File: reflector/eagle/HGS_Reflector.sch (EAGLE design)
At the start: 27 parts, among them J1 U.FL, U3 LP2985XX-N

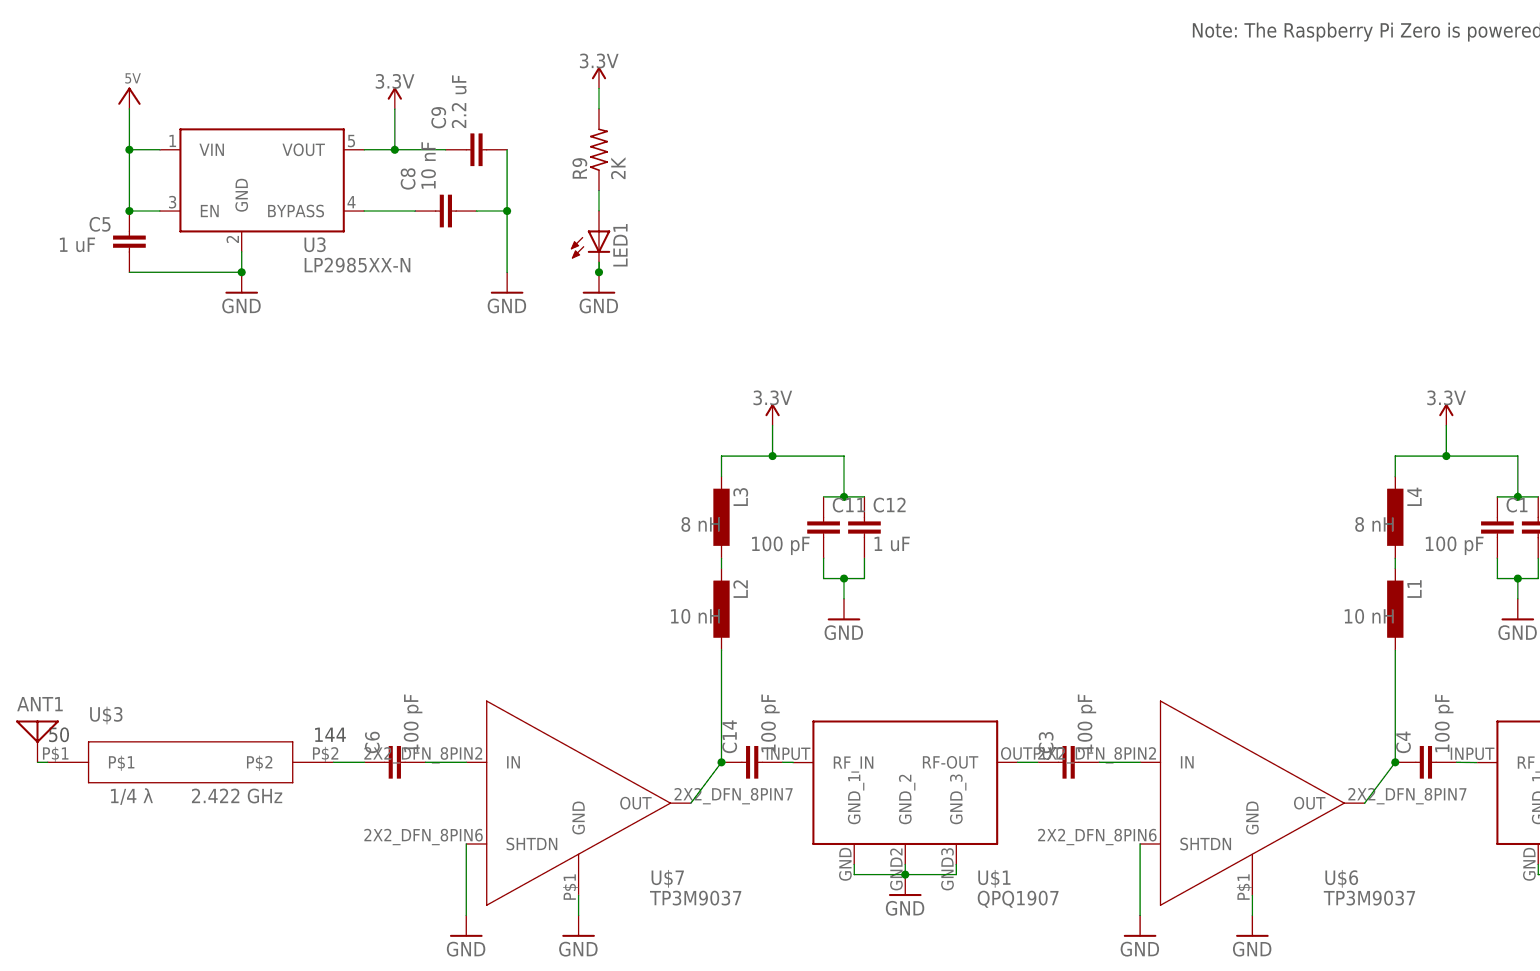
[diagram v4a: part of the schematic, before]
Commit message: Since the team working on HGS decided to switch from a 2 layer board to a 4 layer board, I began laying out the HGS parts on a new board with 4 layers. Currently, I have a number of questions regarding the layout to go over at the 11/29 structure meeting.
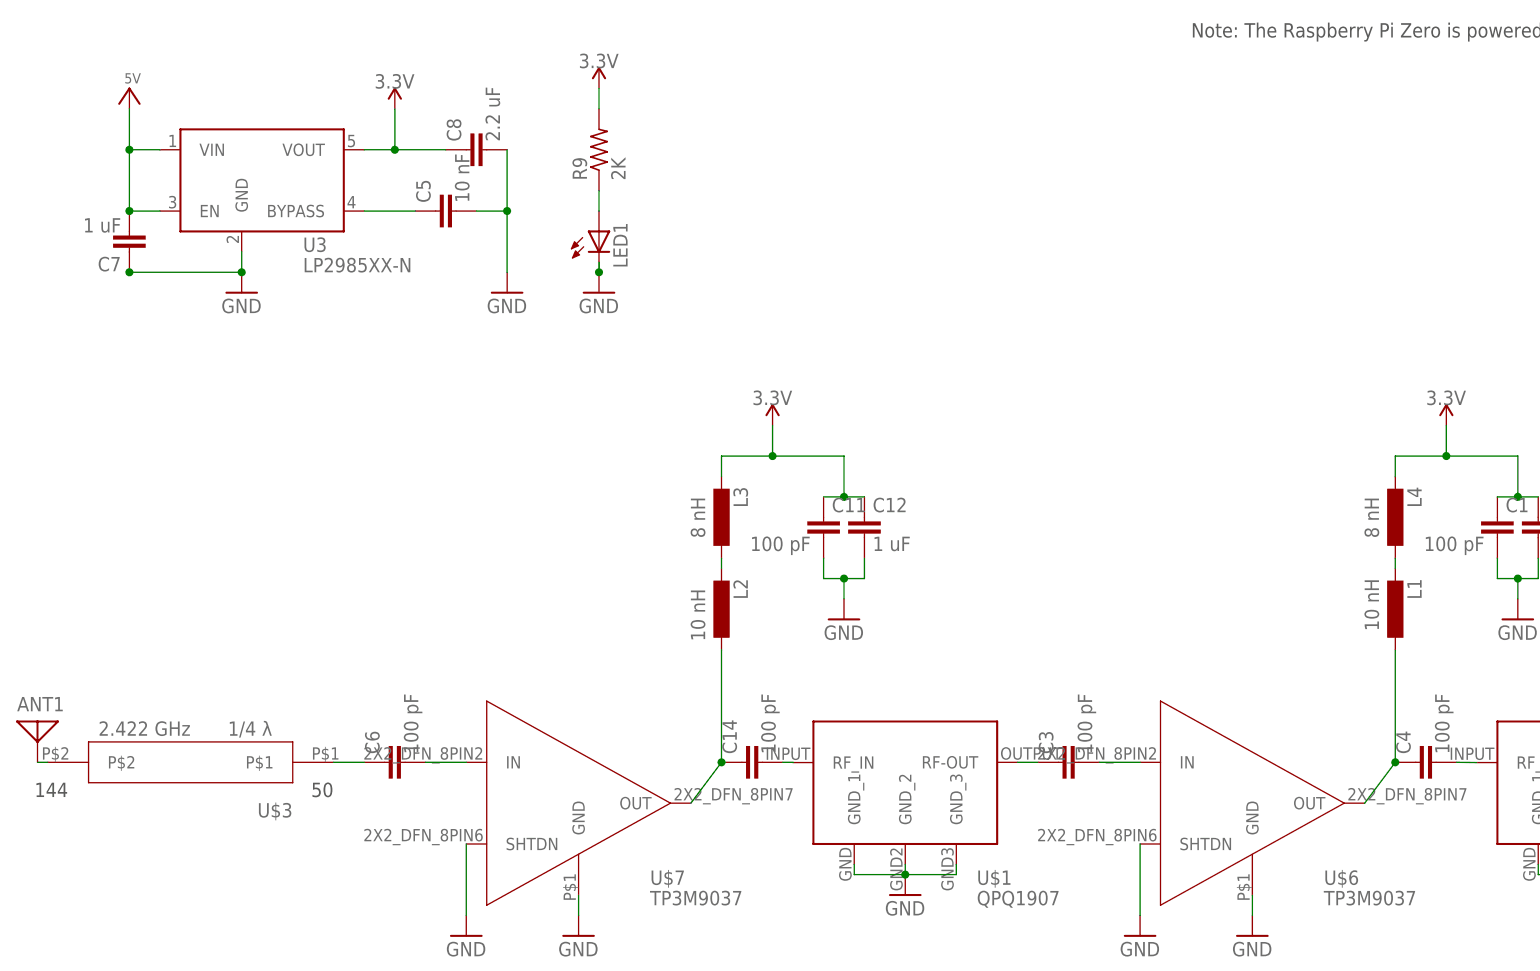
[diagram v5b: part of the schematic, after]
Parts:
- removed C9: 2.2 uF, ngspice-simulation:C
- added C7: 1 uF, oresat-rcl:C-EU0402-C-NOSILK
- C5: value 1 uF -> 10 nF; device ngspice-simulation:C -> oresat-rcl:C-EU0402-C-NOSILK; _EXTERNAL_ 1 uF -> (none)
- C8: value 10 nF -> 2.2 uF; device ngspice-simulation:C -> oresat-rcl:C-EU0402-C-NOSILK
- L1: IMPEDANCE (none) -> 10 nH; SPICEPREFIX 10 nH -> (none)
- L3, L4: IMPEDANCE (none) -> 8 nH; SPICEPREFIX 8 nH -> (none)
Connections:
- removed net N$12: ANT1.1, U$3.P$1
- new net N$2: ANT1.1, U$3.P$2
- net 3.3V: now also C8.1; no longer C9.1
- net 5V: now also C7.2; no longer C5.1
- net GND: now also C7.1; no longer C9.2
- net N$1: now also C5.1; no longer C8.1
- net N$9: now also U$3.P$1; no longer U$3.P$2
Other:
- moved on the sheet: U$3

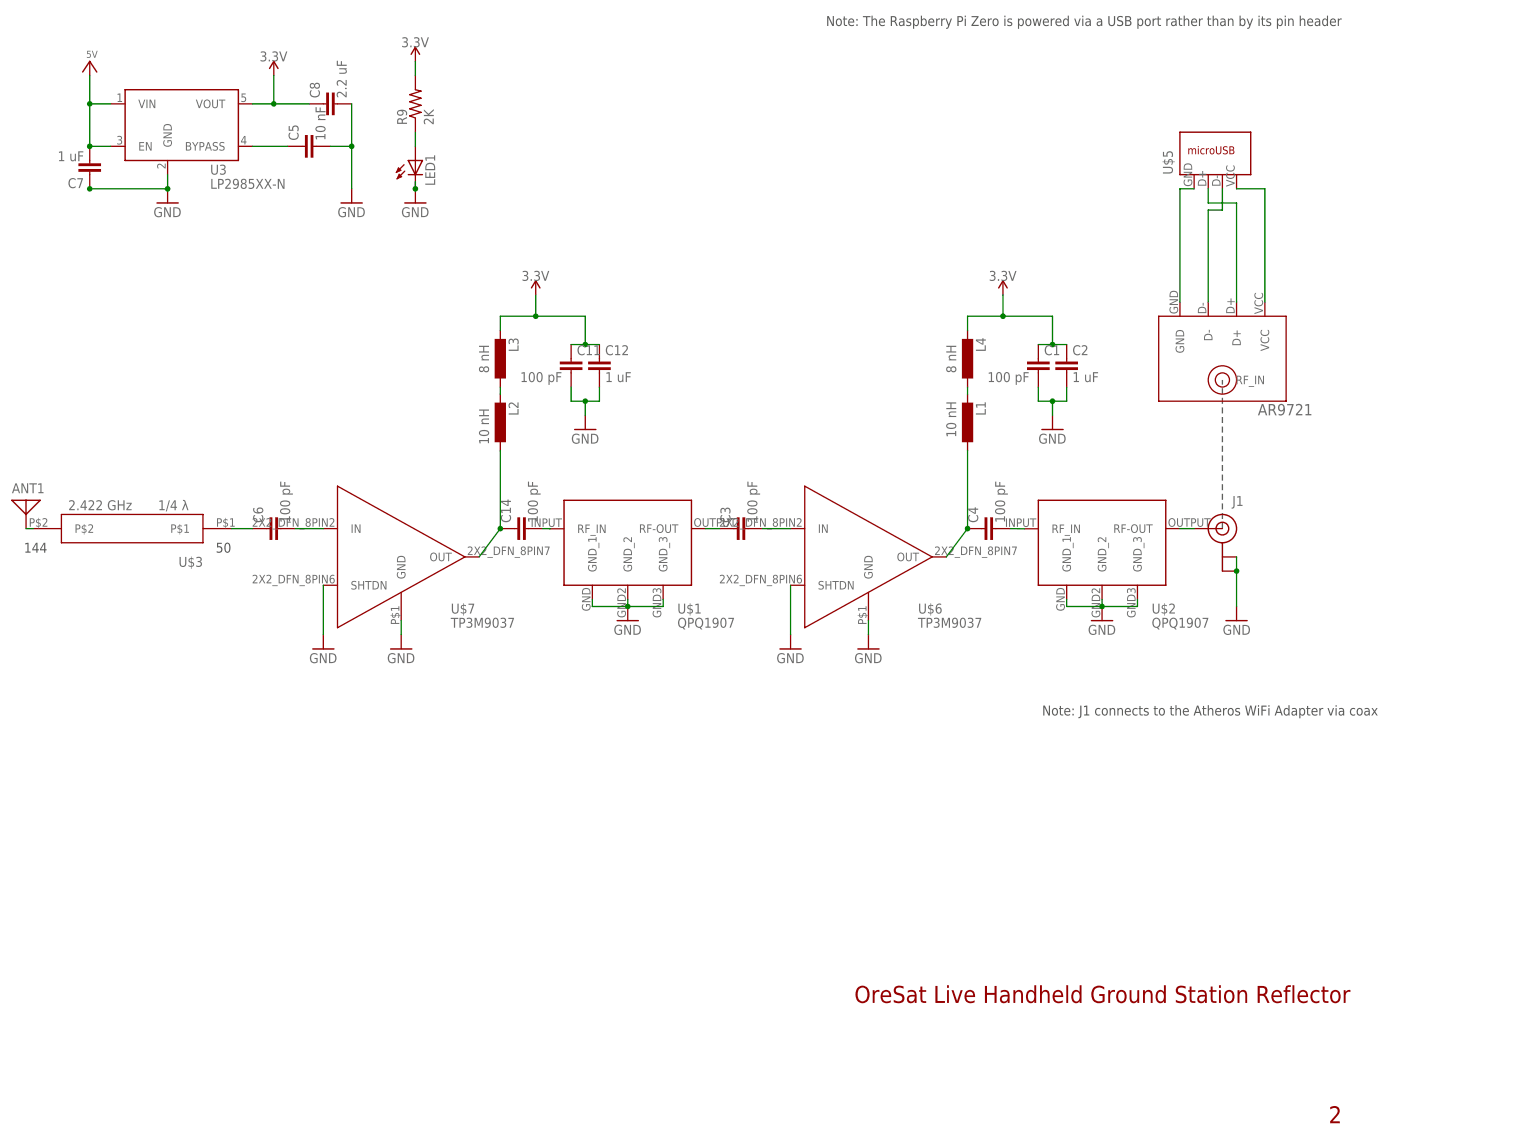
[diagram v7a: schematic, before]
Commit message: I finalized the schematic and routing of the board for HGS. Note that I adjusted the dxf layer by adding a fourth drill hole underneath the atheros card. It is ready for a design review.
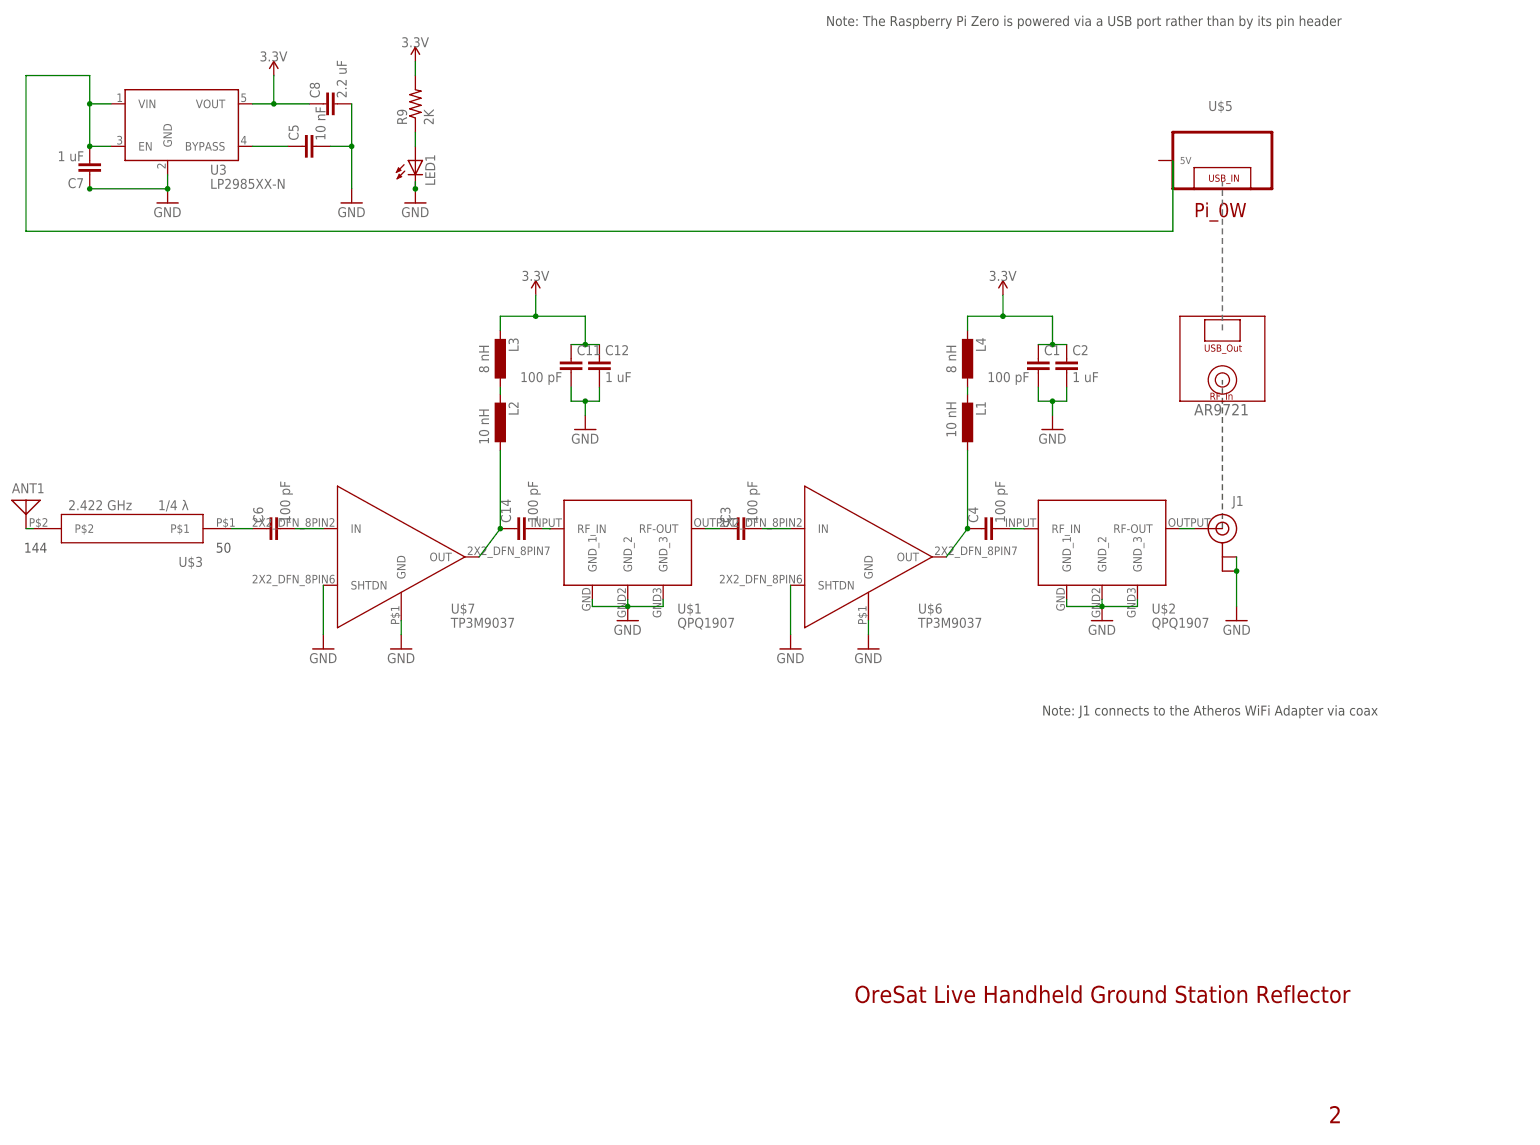
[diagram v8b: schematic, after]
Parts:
- U$4: value AR9721 -> AR9721WF; device AR9721:AR9721 -> AR9721:AR9721WF
- U$5: device Rasp_Pi_0W:RASP_PI_0W -> Rasp_Pi_0W:RASP_PI_0WPI_0W
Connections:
- removed net 1: U$4.GND
- removed net 5V: C7.2, U3.EN, U3.VIN
- removed net N$18: U$4.D+
- removed net N$19: U$4.D-
- removed net VCC: U$4.VCC
- new net N$12: C7.2, U$5.5V, U3.EN, U3.VIN
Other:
- moved on the sheet: U$5
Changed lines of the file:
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@@
 <part name="U3" library="U-TI-LP2985XX-N-linear-reg" deviceset="LP2985XX-N" device=""/>
 <part name="GND5" library="supply1" library_urn="urn:adsk.eagle:library:371" deviceset="GND" device=""/>
-<part name="3V-1" library="oresat-supplies" deviceset="5V" device=""/>
 <part name="GND1" library="supply1" library_urn="urn:adsk.eagle:library:371" deviceset="GND" device=""/>
 <part name="3.3V2" library="oresat-supplies" deviceset="3.3V" device=""/>
@@
 <part name="U$1" library="QPQ1907_BPF" deviceset="BPF" device=""/>
 <part name="U$2" library="QPQ1907_BPF" deviceset="BPF" device=""/>
-<part name="U$4" library="AR9721" deviceset="AR9721" device=""/>
-<part name="U$5" library="Rasp_Pi_0W" deviceset="RASP_PI_0W" device=""/>
+<part name="U$4" library="AR9721" deviceset="AR9721" device="WF"/>
+<part name="U$5" library="Rasp_Pi_0W" deviceset="RASP_PI_0W" device="PI_0W"/>
 <part name="U$3" library="TM-QWT-2.422GHz" deviceset="QWT2.422" device=""/>
 <part name="C7" library="oresat-rcl" deviceset="C-EU" device="0402-C-NOSILK" value="1 uF"/>
@@
 <text x="175.26" y="203.2" size="1.778" layer="97">Note: The Raspberry Pi Zero is powered via a USB port rather than by its pin header</text>
 <text x="274.32" y="81.28" size="1.778" layer="97" rot="R180">Note: J1 connects to the Atheros WiFi Adapter via coax</text>
-<wire x1="246.38" y1="113.03" x2="246.38" y2="139.7" width="0.1524" layer="97" style="shortdash"/>
+<wire x1="246.38" y1="113.03" x2="246.38" y2="139.7" width="0.254" layer="97" style="shortdash"/>
+<wire x1="246.38" y1="148.59" x2="246.38" y2="175.26" width="0.254" layer="95" style="shortdash"/>
 </plain>
 <instances>
@@
 <attribute name="VALUE" x="54.61" y="168.91" size="1.778" layer="96"/>
 </instance>
-<instance part="3V-1" gate="G$1" x="43.18" y="196.85" smashed="yes">
-<attribute name="VALUE" x="42.545" y="197.485" size="1.27" layer="96"/>
-</instance>
 <instance part="GND1" gate="1" x="99.06" y="91.44" smashed="yes">
 <attribute name="VALUE" x="96.52" y="88.9" size="1.778" layer="96"/>
@@
 </instance>
 <instance part="U$4" gate="G$1" x="246.38" y="143.51" smashed="yes"/>
-<instance part="U$5" gate="G$1" x="246.38" y="179.07" smashed="yes" rot="R90">
-<attribute name="NAME" x="237.49" y="176.53" size="1.778" layer="95" rot="R90"/>
-<attribute name="VALUE" x="254" y="176.53" size="1.778" layer="96" rot="R90"/>
+<instance part="U$5" gate="G$1" x="246.38" y="179.07" smashed="yes">
+<attribute name="NAME" x="243.84" y="187.96" size="1.778" layer="95"/>
+<attribute name="VALUE" x="243.84" y="171.45" size="1.778" layer="96"/>
 </instance>
 <instance part="U$3" gate="G$1" x="50.8" y="113.03" smashed="yes" rot="R180">
@@
 </segment>
 </net>
-<net name="1" class="0">
-<segment>
-<wire x1="238.76" y1="153.67" x2="238.76" y2="173.99" width="0.1524" layer="91"/>
-<wire x1="238.76" y1="173.99" x2="241.3" y2="173.99" width="0.1524" layer="91"/>
-<pinref part="U$4" gate="G$1" pin="GND"/>
-</segment>
-</net>
 <net name="N$16" class="0">
 <segment>
@@
 </segment>
 </net>
-<net name="N$18" class="0">
-<segment>
-<wire x1="243.84" y1="173.99" x2="243.84" y2="171.45" width="0.1524" layer="91"/>
-<wire x1="243.84" y1="171.45" x2="248.92" y2="171.45" width="0.1524" layer="91"/>
-<wire x1="248.92" y1="171.45" x2="248.92" y2="153.67" width="0.1524" layer="91"/>
-<pinref part="U$4" gate="G$1" pin="D+"/>
-</segment>
-</net>
-<net name="N$19" class="0">
-<segment>
-<wire x1="243.84" y1="153.67" x2="243.84" y2="170.18" width="0.1524" layer="91"/>
-<wire x1="243.84" y1="170.18" x2="246.38" y2="170.18" width="0.1524" layer="91"/>
-<wire x1="246.38" y1="170.18" x2="246.38" y2="173.99" width="0.1524" layer="91"/>
-<pinref part="U$4" gate="G$1" pin="D-"/>
-</segment>
-</net>
-<net name="5V" class="1">
-<segment>
-<pinref part="U3" gate="G$1" pin="VIN"/>
-<wire x1="46.99" y1="189.23" x2="43.18" y2="189.23" width="0.1524" layer="91"/>
-<wire x1="43.18" y1="181.61" x2="43.18" y2="189.23" width="0.1524" layer="91"/>
-<pinref part="U3" gate="G$1" pin="EN"/>
-<wire x1="46.99" y1="181.61" x2="43.18" y2="181.61" width="0.1524" layer="91"/>
-<pinref part="3V-1" gate="G$1" pin="5V"/>
-<wire x1="43.18" y1="189.23" x2="43.18" y2="194.31" width="0.1524" layer="91"/>
-<junction x="43.18" y="189.23"/>
-<pinref part="C7" gate="CE" pin="2"/>
-<junction x="43.18" y="181.61"/>
-</segment>
-</net>
 <net name="N$4" class="0">
 <segment>
@@
 </segment>
 </net>
-<net name="VCC" class="0">
-<segment>
-<wire x1="248.92" y1="173.99" x2="254" y2="173.99" width="0.1524" layer="91"/>
-<wire x1="254" y1="173.99" x2="254" y2="153.67" width="0.1524" layer="91"/>
-<pinref part="U$4" gate="G$1" pin="VCC"/>
-</segment>
-</net>
 <net name="N$2" class="0">
 <segment>
@@
 </segment>
 </net>
+<net name="N$12" class="1">
+<segment>
+<pinref part="U3" gate="G$1" pin="VIN"/>
+<wire x1="46.99" y1="189.23" x2="43.18" y2="189.23" width="0.1524" layer="91"/>
+<wire x1="43.18" y1="181.61" x2="43.18" y2="189.23" width="0.1524" layer="91"/>
+<pinref part="U3" gate="G$1" pin="EN"/>
+<wire x1="46.99" y1="181.61" x2="43.18" y2="181.61" width="0.1524" layer="91"/>
+<wire x1="43.18" y1="189.23" x2="43.18" y2="194.31" width="0.1524" layer="91"/>
+<junction x="43.18" y="189.23"/>
+<pinref part="C7" gate="CE" pin="2"/>
+<junction x="43.18" y="181.61"/>
+<wire x1="43.18" y1="194.31" x2="31.75" y2="194.31" width="0.1524" layer="91"/>
+<wire x1="31.75" y1="194.31" x2="31.75" y2="166.37" width="0.1524" layer="91"/>
+<pinref part="U$5" gate="G$1" pin="5V"/>
+<wire x1="31.75" y1="166.37" x2="237.49" y2="166.37" width="0.1524" layer="91"/>
+<wire x1="237.49" y1="166.37" x2="237.49" y2="179.07" width="0.1524" layer="91"/>
+</segment>
+</net>
